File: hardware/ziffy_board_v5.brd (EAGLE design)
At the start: 52 x 42 mm, 22 parts, among them IC1 ATMEGA328P, Q1 2N3904, Q2 2N3904

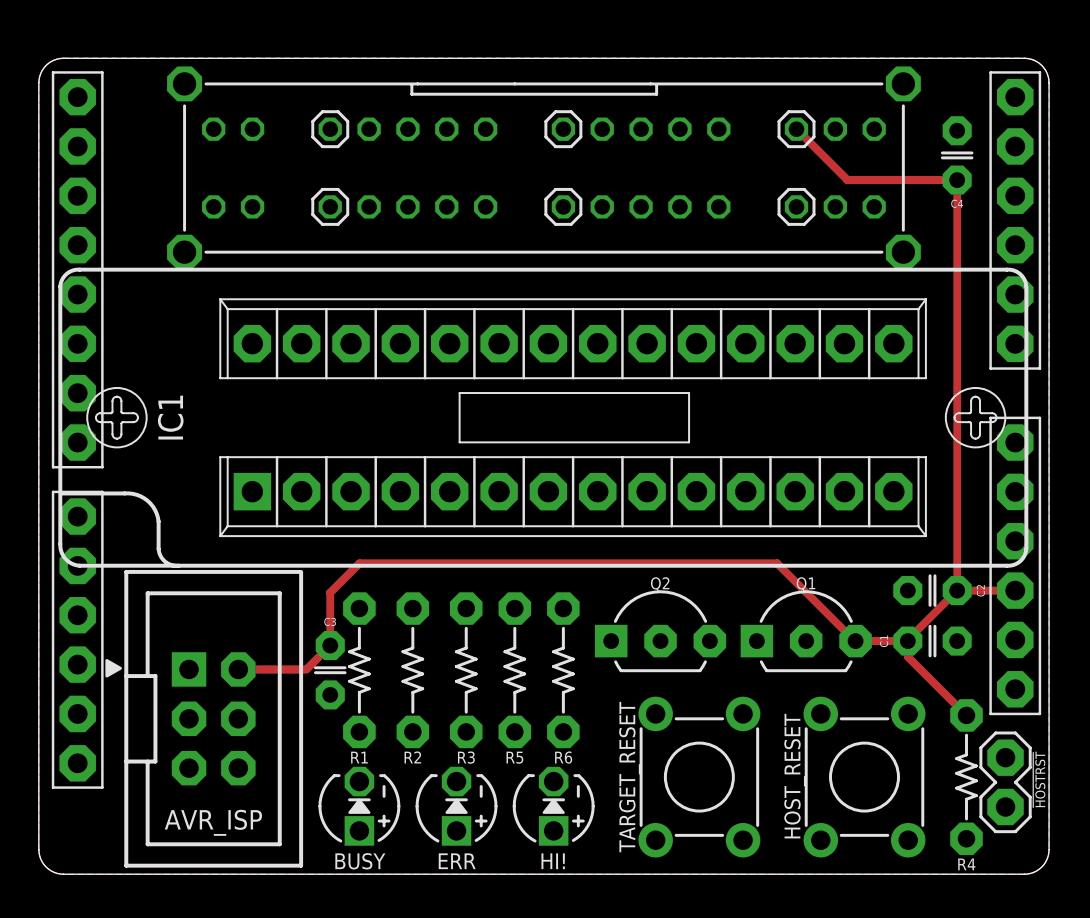
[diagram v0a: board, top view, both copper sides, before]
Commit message: most routing complete, just the ratsnest near the switch left (ugh)
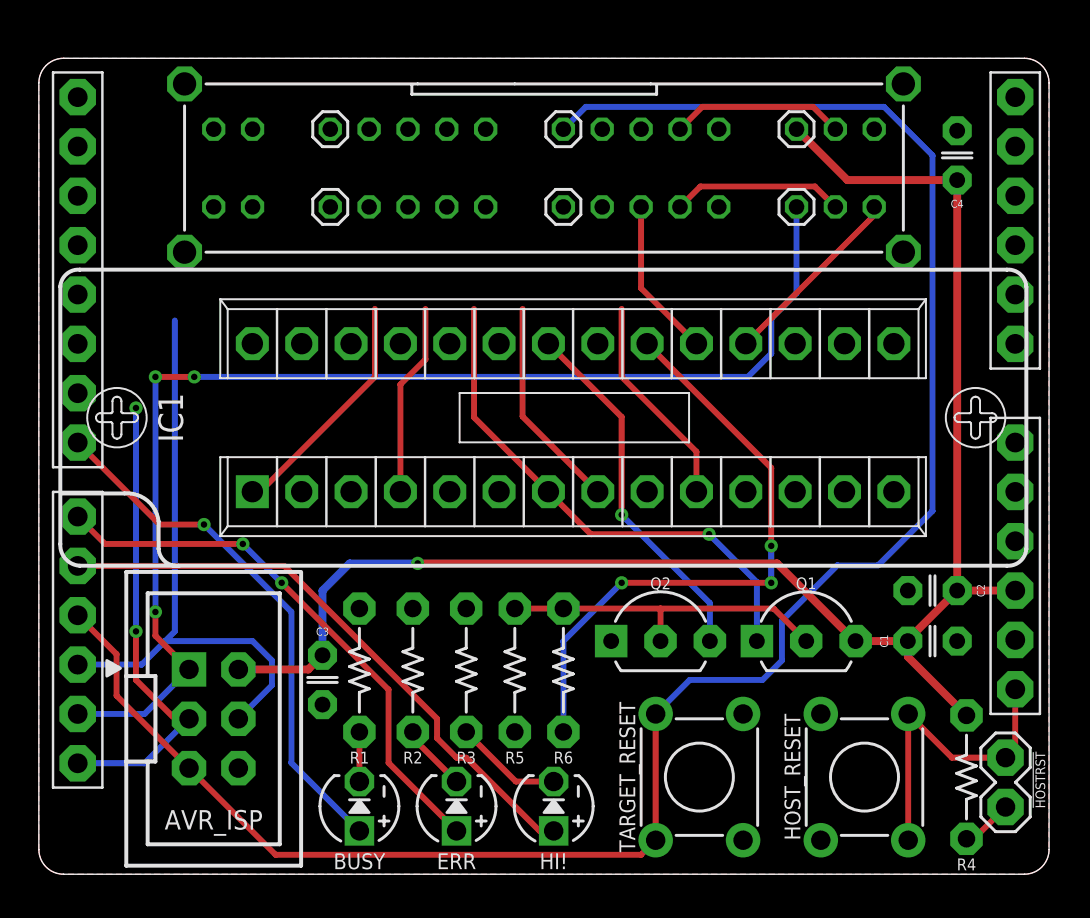
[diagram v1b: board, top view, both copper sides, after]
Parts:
- moved C3 0.64 mm to (14.6, 10.0)
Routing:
- net TAR_RST: track 0.00 -> 101.5 mm
- net MISO: track 0.00 -> 62.7 mm, vias 0 -> 3
- net Z20: track 0.00 -> 31.6 mm, vias 0 -> 3
- net MOSI: track 0.00 -> 31.3 mm
- net HELLO: track 0.00 -> 30.7 mm
- net ERROR: track 0.00 -> 28.4 mm, vias 0 -> 2
- net BUSY: track 0.00 -> 27.3 mm, vias 0 -> 1
- net Z7: track 0.00 -> 26.7 mm, vias 0 -> 1
- net SCK: track 0.00 -> 24.2 mm, vias 0 -> 2
- net Z22: track 0.00 -> 18.8 mm, vias 0 -> 1
- net N$21: track 0.00 -> 17.4 mm
- net HOST_RESET: track 0.00 -> 16.0 mm
- net Z1: track 0.00 -> 12.3 mm
- net Z8: track 0.00 -> 11.0 mm
- net Z10: track 0.00 -> 11.0 mm
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
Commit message: layout complete for mark 5
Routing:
- net Z28: track 8.95 -> 39.7 mm, vias 0 -> 1
- net SCK: track 24.2 -> 53.5 mm, vias 2 -> 4
- net Z4: track 9.94 -> 38.4 mm, vias 0 -> 2
- net Z1: track 12.3 -> 40.3 mm, vias 0 -> 2
- net Z17: track 0.00 -> 27.3 mm, vias 0 -> 2
- net Z27: track 0.00 -> 22.7 mm, vias 0 -> 2
- net Z26: track 8.87 -> 29.8 mm
- net Z25: track 0.00 -> 20.8 mm
- net Z7: track 26.7 -> 46.6 mm, vias 1 -> 3
- net Z20: track 31.6 -> 49.8 mm
- net Z10: track 11.0 -> 28.0 mm, vias 0 -> 2
- net MOSI: track 31.3 -> 47.2 mm, vias 0 -> 1
- net Z22: track 18.8 -> 33.8 mm, vias 1 -> 3
- net Z8: track 11.0 -> 22.2 mm, vias 0 -> 2
- net Z23: track 0.00 -> 7.33 mm
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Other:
- board size 52 x 42 mm -> 52 x 43 mm
- board text added: "ATMEGA328P"
- board text added: "ATTINY2313"
- board text added: "ATTINY84"
- board text added: "ATTINY85"

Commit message: touch ups, edge routering, etc.
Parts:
- C3: value 0.1uF -> 1uF
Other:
- board size 52 x 43 mm -> 52 x 42.5 mm

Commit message: silk screen, ready for fab i think
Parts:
- added U$1, U$5: (no value), A_butts:CC-BY-SA-4.0-NO-URL
- added U$2: (no value), A_butts:COW
- added U$3: (no value), A_butts:OSHWLOGO_BOT_0.2
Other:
- board text added: ""ZIFFY" AVR ISP"
- board text added: "Rev 5.0"
- board text added: "by schizobovine <sean@yak.net>"
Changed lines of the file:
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@@
 <vertex x="10" y="17"/>
 </polygon>
+<text x="27.5" y="17" size="1.27" layer="22" font="vector" ratio="12" rot="MR0" align="top-center">"ZIFFY" AVR ISP</text>
+<text x="27.5" y="15.5" size="0.8128" layer="22" font="vector" ratio="12" rot="MR0" align="top-center">Rev 5.0</text>
+<text x="22.8" y="11.6" size="0.6096" layer="22" font="vector" ratio="12" rot="MR0" align="top-center">by schizobovine
+&lt;sean@yak.net&gt;</text>
+<text x="2.5" y="4" size="0.6096" layer="21" font="vector" ratio="12" align="top-center">Rev 5.0</text>
 </plain>
 <attributes>
@@
 <attribute name="VALUE" x="24.5" y="14.691" size="0.5" layer="21" font="vector" ratio="12" rot="R180" align="top-center"/>
 </element>
+<element name="U$1" library="A_butts" package="CC-BY-SA-4.0-NO-URL" value="" x="5.4" y="36.4" rot="R270"/>
+<element name="U$2" library="A_butts" package="COW" value="" x="27.5" y="23.5" rot="MR0"/>
+<element name="U$3" library="A_butts" package="OSHWLOGO_BOT_0.2" value="" x="42.8" y="23.4"/>
+<element name="U$5" library="A_butts" package="CC-BY-SA-4.0-NO-URL" value="" x="16" y="23.5" rot="MR0"/>
 </elements>
 <signals>
@@
 </board>
 </drawing>
+<compatibility>
+<note version="6.3" minversion="6.2.2" severity="warning">
+Since Version 6.2.2 text objects can contain more than one line,
+which will not be processed correctly with this version.
+</note>
+</compatibility>
 </eagle>
